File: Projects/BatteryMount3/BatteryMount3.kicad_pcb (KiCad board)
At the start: 2 copper layers, 37 parts

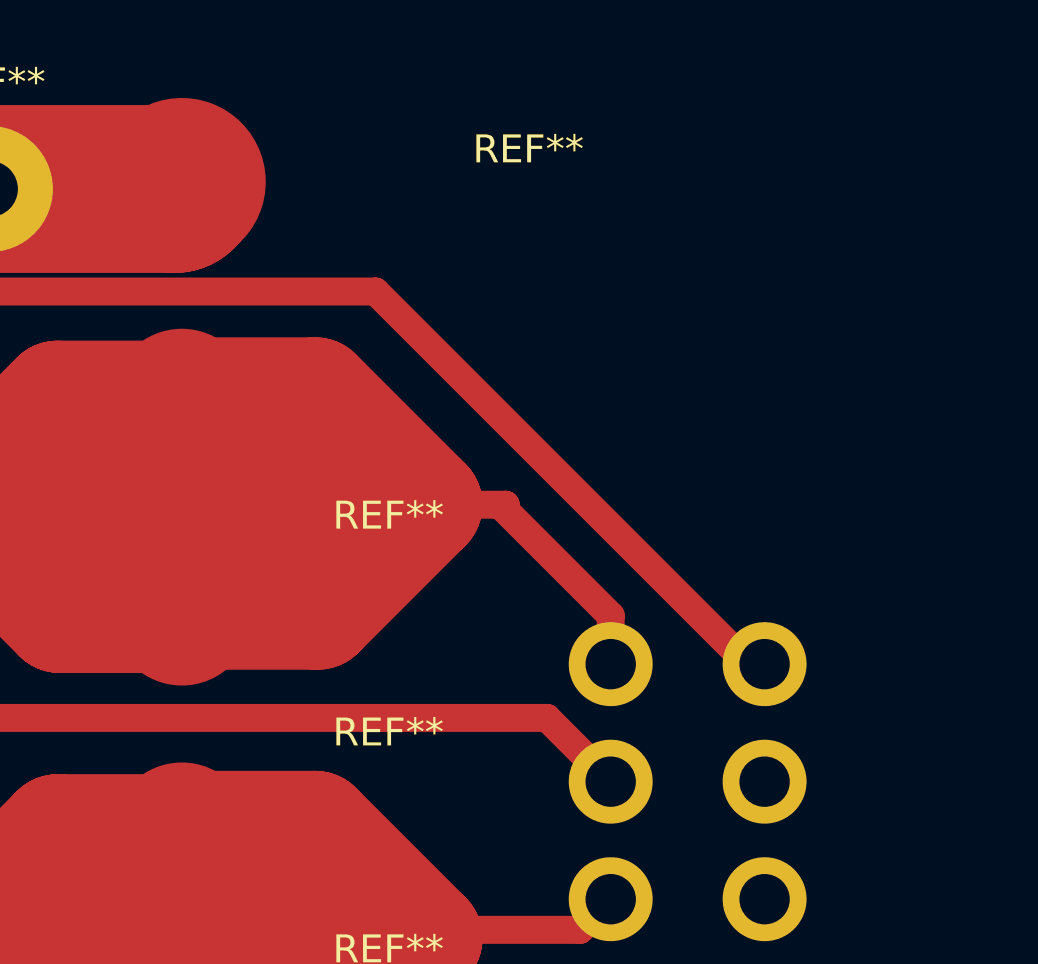
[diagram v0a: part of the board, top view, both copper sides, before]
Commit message: editted batterymount3
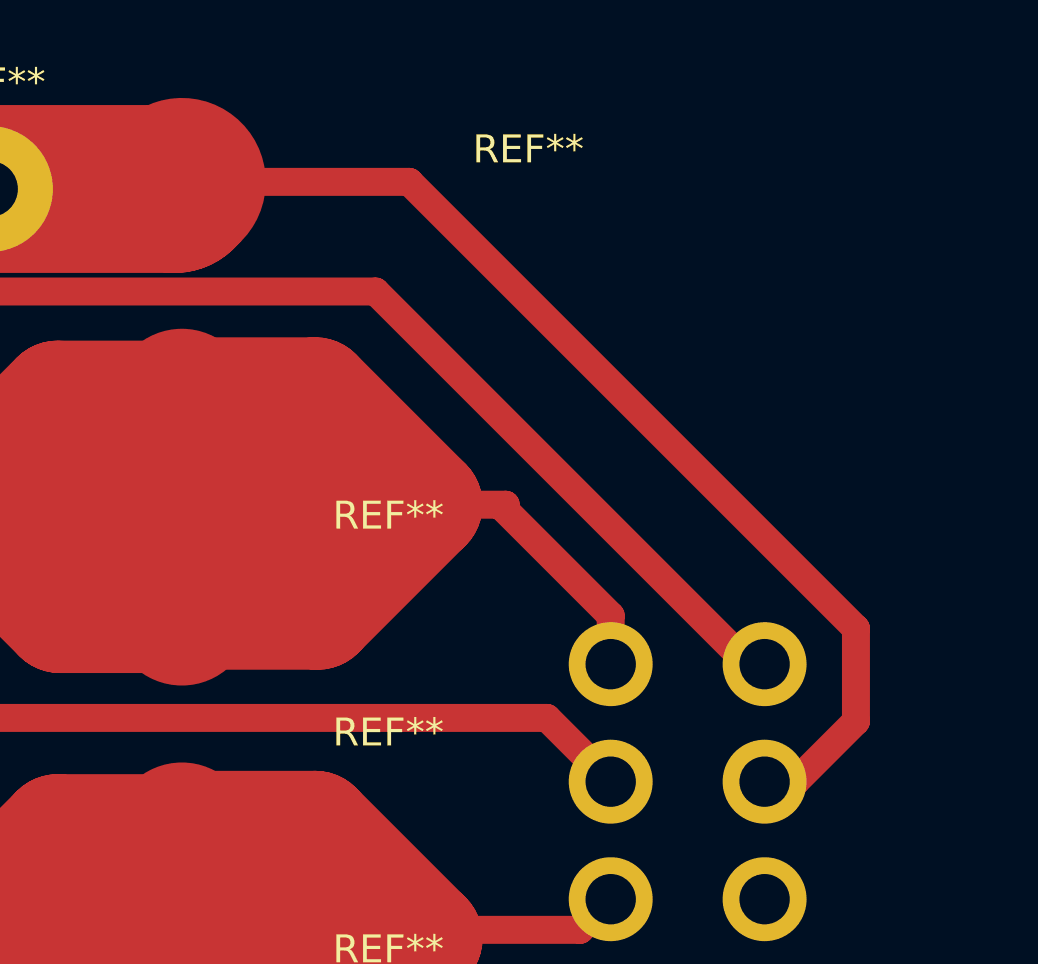
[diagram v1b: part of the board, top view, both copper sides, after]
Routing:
- net (no net): track 1256.8 -> 1295.0 mm
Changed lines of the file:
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@@
     (thickness 1.6)
     (drawings 13)
-    (tracks 191)
+    (tracks 196)
     (zones 0)
     (modules 37)
@@
   (gr_line (start 0 -0.508) (end 0 62) (layer B.Paste) (width 0.2))
   (gr_line (start 0 -0.5) (end 160 -0.5) (layer B.Paste) (width 0.2))
+  (segment (start 134.622 3.556) (end 142.750047 3.556) (width 1) (layer F.Cu) (net 0))
+  (segment (start 142.750047 3.556) (end 158.712908 19.518861) (width 1) (layer F.Cu) (net 0))
+  (segment (start 158.712908 19.518861) (end 158.712908 22.83521) (width 1) (layer F.Cu) (net 0))
+  (segment (start 158.712908 22.83521) (end 156.556118 24.992) (width 1) (layer F.Cu) (net 0))
+  (segment (start 156.556118 24.992) (end 155.448 24.992) (width 1) (layer F.Cu) (net 0))
   (segment (start 127.762 57.912) (end 134.516 57.912) (width 6) (layer F.Cu) (net 0))
   (segment (start 134.516 57.912) (end 134.622 57.806) (width 6) (layer F.Cu) (net 0))
